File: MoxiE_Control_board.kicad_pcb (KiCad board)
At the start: 2 copper layers, 90 x 50 mm, 144 parts, among them J101 USB_B_Micro, J301 SWD, J401 Conn_01x02, J402 Conn_01x02, J403 Conn_01x02, K101 SERVO, P101 CANBUS, P102 Serial3, P103 CTRL_SIGNALS, P104 SPI, P105 Serial1/tim4, P106 I2C, P107 HALL/Encoder, Q401 IRLML6344TRPBF, Q402 IRLML6344TRPBF, Q701 TPH2R608NH,L1Q, Q702 TPH2R608NH,L1Q, Q703 TPH2R608NH,L1Q, Q704 TPH2R608NH,L1Q, Q801 TPH2R608NH,L1Q, Q802 TPH2R608NH,L1Q, Q803 TPH2R608NH,L1Q, Q804 TPH2R608NH,L1Q, Q901 TPH2R608NH,L1Q, Q902 TPH2R608NH,L1Q, Q903 TPH2R608NH,L1Q, Q904 TPH2R608NH,L1Q, U201 TJA1051TK-3, U301 STM32F40X_LQFP64, U501 TPS561201, U601 DRV8353RSRGZT, X301 8MHz 10ppm

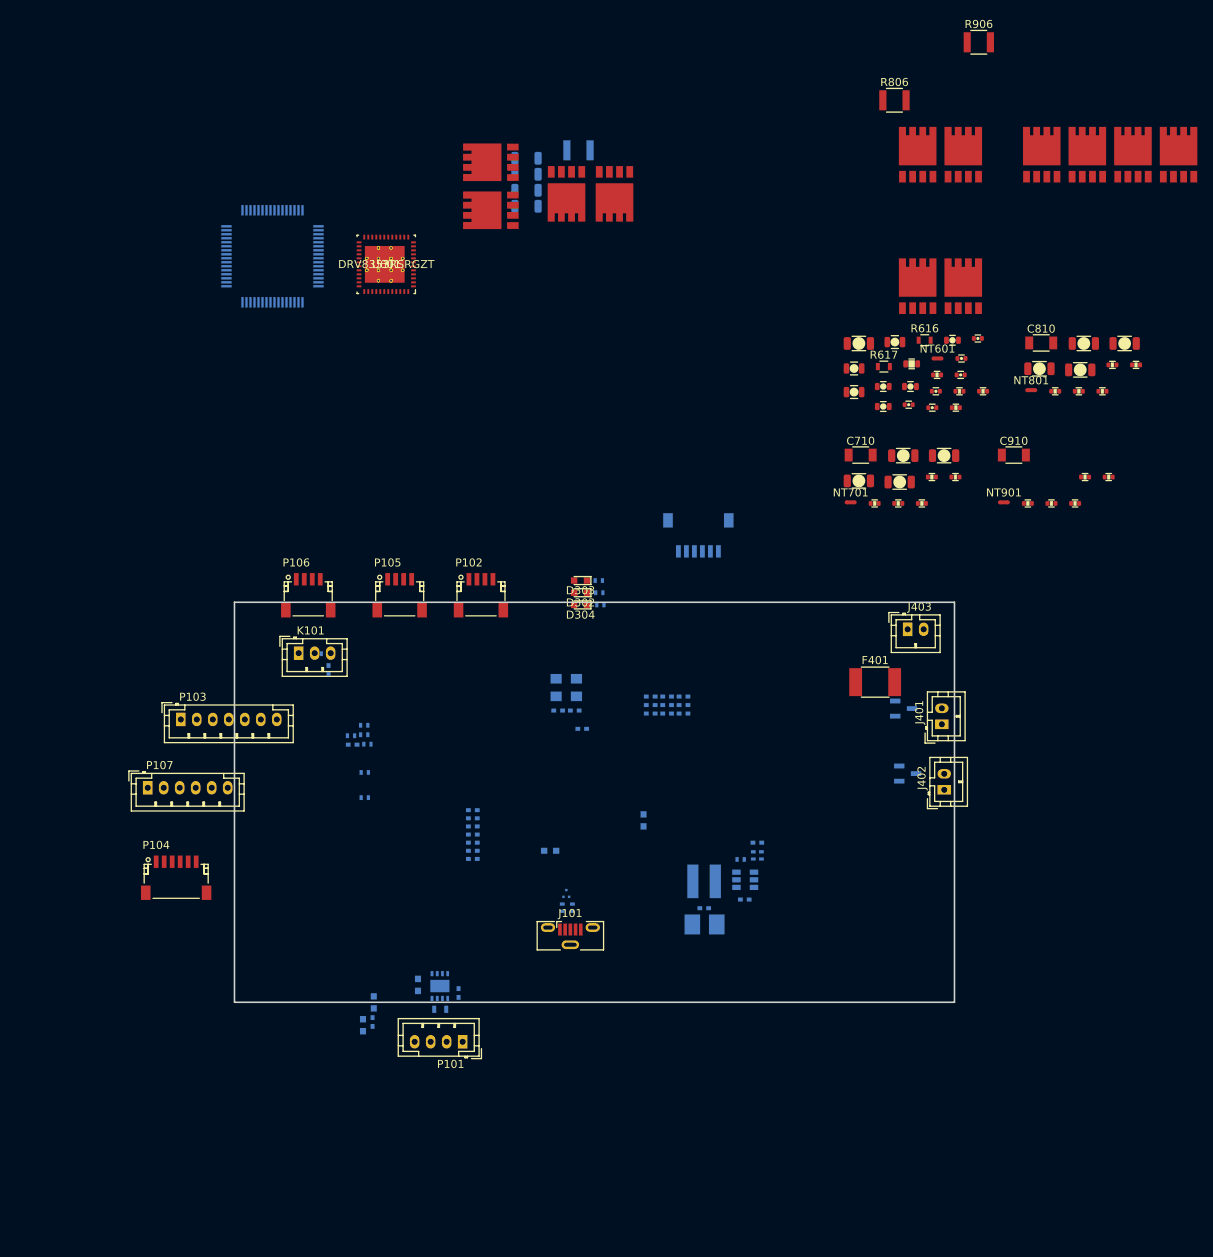
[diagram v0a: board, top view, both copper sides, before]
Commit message: further progress finalising schematic and power stage laied out. drv is fanned out, and logic is starting to be routed
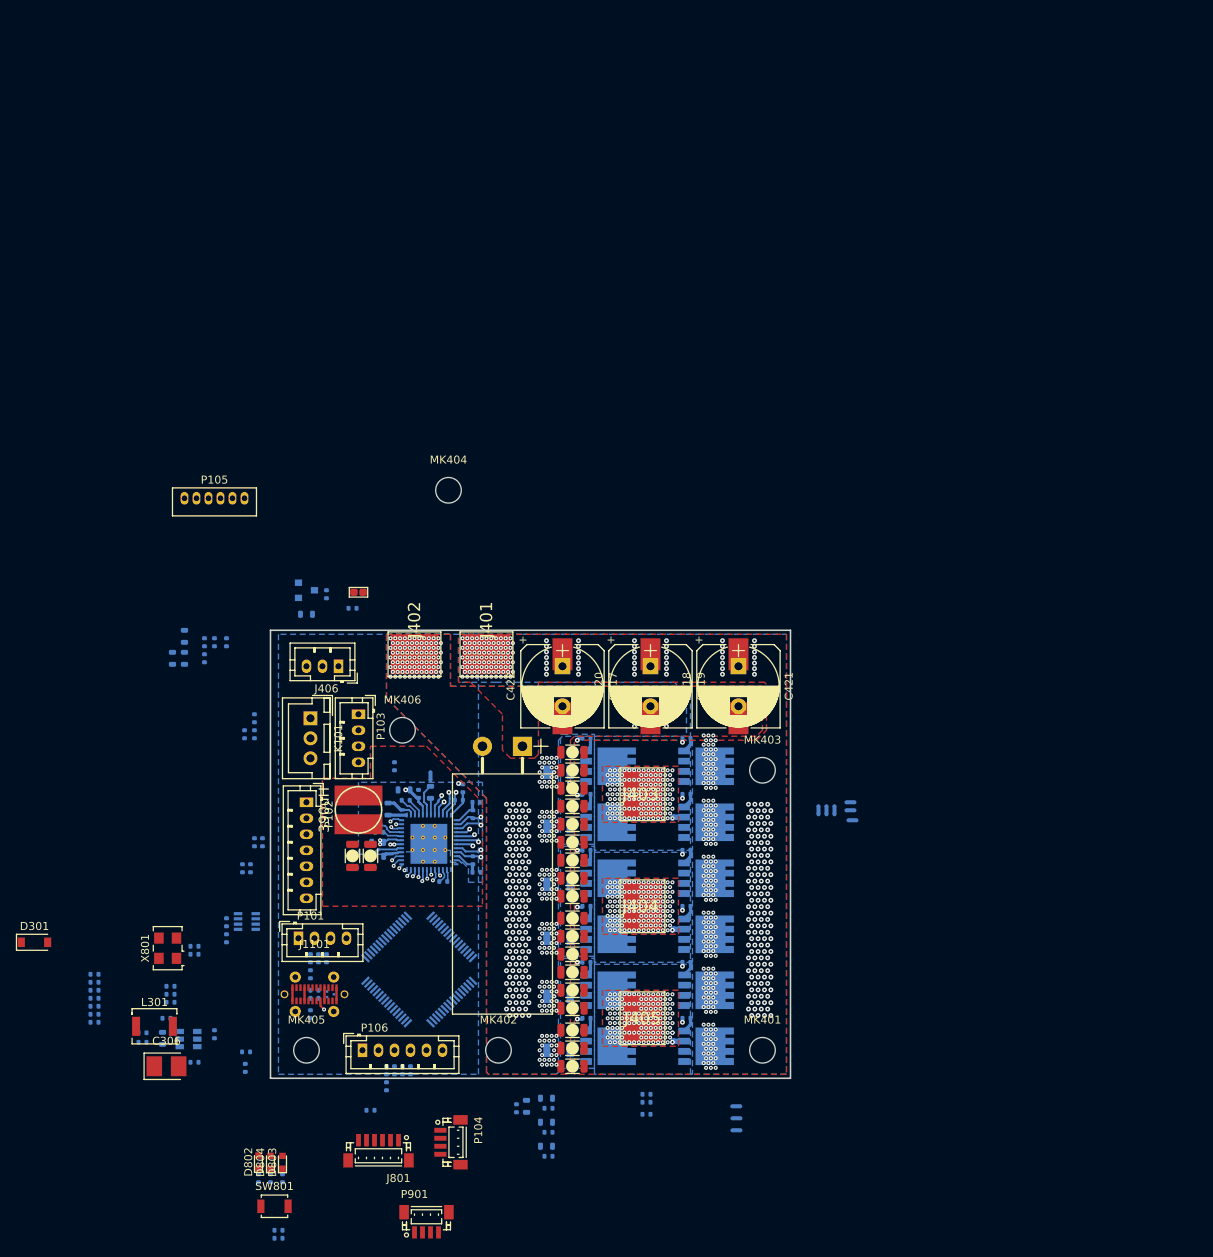
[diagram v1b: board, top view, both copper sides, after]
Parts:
- removed C103, C104, C105: 4.7nf, Capacitors_SMD:C_0402
- removed C106, C107, C108, C109, C111: 100nf, Capacitors_SMD:C_0402
- removed C110: 100n, Capacitors_SMD:C_0402
- removed C308: 15p, Capacitors_SMD:C_0402
- removed C309, C310, C311, C312: 2.2u, Capacitors_SMD:C_0402
- removed C623: 10uF, pkl_dipol:C_0805
- removed C624: 1.5uF, pkl_dipol:C_1206
- removed C625: 0.1uF, pkl_dipol:C_0603
- removed C626: 0.1uF, pkl_dipol:C_0805
- removed C627: 0.47uF, pkl_dipol:C_0402
- removed C629: 0.047uF, pkl_dipol:C_0402
- removed C630, C631, C633: 1uF, pkl_dipol:C_0603
- removed C632: 0.01uF, pkl_dipol:C_0402
- removed C634: 18nF, pkl_dipol:C_0402
- removed C635: 22uF, pkl_dipol:C_0805
- removed C710, C910: 100v_1.0uF, Capacitors_SMD:C_1206
- removed C902, C903, C904, C905: 1uF, pkl_dipol:C_1206
- removed D302: BLUE, LEDs:LED_0603
- removed D303: GREEN, LEDs:LED_0603
- removed D304: RED, LEDs:LED_0603
- removed F401: 0.5A polyfuse, Resistors_SMD:R_1812
- removed J101: USB_B_Micro, Connectors_USB:USB_Micro-B_Vertical_Molex-105133-0001
- removed J301: SWD, Connectors_JST:JST_SH_SM06B-SRSS-TB_06x1.00mm_Angled
- removed L501: 3.3uH, Mas_custom_parts:L_Bourns_SRN-4018
- removed NT801, NT901: Net-Tie_2, NetTie:NetTie-2_SMD_Pad0.5mm
- removed P107: HALL/Encoder, Connectors_JST:JST_PH_B6B-PH-K_06x2.00mm_Straight
- removed Q402: IRLML6344TRPBF, digikey-footprints:SOT-23-3
- removed Q802, Q901, Q902, Q903, Q904: TPH2R608NH,L1Q, moxie-drive-custom:SOP8_Advance
- removed R105: 22R, Resistors_SMD:R_0402
- removed R106: 2k2, Resistors_SMD:R_0402
- removed the R502 at (164.9, 131.6)
- removed the R503 at (165.9, 131.6)
- removed the R603 at (190.2, 75.7)
- removed R616: 39k, Resistors_SMD:R_0603
- removed R617: 2k2, Resistors_SMD:R_0603
- removed the R703 at (183.0, 87.6)
- removed R805, R901, R902, R904, R905: 5Ω, pkl_dipol:R_0402
- removed R806, R906: 0.5mΩ, Resistors_SMD:R_1210
- removed R903: 100Ω, pkl_dipol:R_0402
- removed U501: TPS561201, TO_SOT_Packages_SMD:SOT-23-6
- removed U601: DRV8353RSRGZT, Locals:DRV8353RHRGZR
- removed X301: 8MHz 10ppm, Oscillators:Oscillator_SMD_EuroQuartz_XO53-4pin_5.0x3.2mm
- added C401: 10uF, pkl_dipol:C_0603, B.Cu at (121.2, 123.5)
- added C402: 10uF, pkl_dipol:C_0603, B.Cu at (93.8, 107.0)
- added C403: 0.1uF, pkl_dipol:C_0402, B.Cu at (123.0, 124.0)
- added C404: 0.1uF, pkl_dipol:C_0603, B.Cu at (117.9, 130.0)
- added C405: 0.47uF, pkl_dipol:C_0402, B.Cu at (118.1, 128.8)
- added C406: 0.1uF, pkl_dipol:C_0402, B.Cu at (126.1, 134.9)
- added C407: 0.047uF, pkl_dipol:C_0402, B.Cu at (121.4, 124.8)
- added C408: 1uF, pkl_dipol:C_0603, B.Cu at (119.2, 125.8)
- added C409: 1uF, pkl_dipol:C_0603, B.Cu at (117.9, 131.8)
- added C410: 0.01uF, pkl_dipol:C_0402, B.Cu at (117.8, 127.8)
- added C411: 1uF, pkl_dipol:C_0603, B.Cu at (124.5, 123.8)
- added C412: 18nF, pkl_dipol:C_0402, B.Cu at (97.5, 105.0)
- added C413: 10uF, pkl_dipol:C_0603, B.Cu at (92.2, 107.0)
- added C414: 560uF, moxie-drive-custom:CP_Radial_D12.5mm_P5.00mm_horiz, F.Cu at (136.0, 118.0)
- added C417: 56uF, Capacitors_THT:CP_Radial_D10.0mm_P5.00mm, F.Cu at (141.0, 108.0)
- added C418: 20uF, Capacitors_SMD:CP_Elec_10x10.5, F.Cu at (163.0, 110.5)
- added C419: 56uF, Capacitors_THT:CP_Radial_D10.0mm_P5.00mm, F.Cu at (152.0, 108.0)
- added C420: 20uF, Capacitors_SMD:CP_Elec_10x10.5, F.Cu at (152.0, 110.5)
- added C421: 56uF, Capacitors_THT:CP_Radial_D10.0mm_P5.00mm, F.Cu at (163.0, 108.0)
- added C422: 20uF, Capacitors_SMD:CP_Elec_10x10.5, F.Cu at (141.0, 110.5)
- added C423: 100nf, pkl_dipol:C_0402, B.Cu at (151.5, 161.5)
- added C424: 1uF, pkl_dipol:C_1206, F.Cu at (117.0, 131.7)
- added C425: 1uF, pkl_dipol:C_1206, F.Cu at (114.8, 131.7)
- added C601: 2.2nF, pkl_dipol:C_0402, B.Cu at (129.8, 126.5)
- added C605: 1uF, pkl_dipol:C_1206, F.Cu at (142.2, 139.5)
- added C606: 1uF, pkl_dipol:C_1206, F.Cu at (142.2, 134.5)
- added C607: 1uF, pkl_dipol:C_1206, F.Cu at (142.2, 136.8)
- added C701: 2.2nF, pkl_dipol:C_0402, B.Cu at (128.1, 124.8)
- added C702: 1uF, pkl_dipol:C_1206, F.Cu at (142.2, 118.8)
- added C703: 1uF, pkl_dipol:C_1206, F.Cu at (142.2, 127.8)
- added C704: 1uF, pkl_dipol:C_1206, F.Cu at (142.2, 130.0)
- added C706: 1uF, pkl_dipol:C_1206, F.Cu at (142.2, 121.0)
- added C707: 1uF, pkl_dipol:C_1206, F.Cu at (142.2, 123.2)
- added C801: 2.2u, pkl_dipol:C_0402, B.Cu at (101.5, 156.2)
- added C806: 15p, pkl_dipol:C_0402, B.Cu at (95.0, 143.0)
- added C807: 2.2u, pkl_dipol:C_0402, B.Cu at (82.5, 149.5)
- added C808: 15p, pkl_dipol:C_0402, B.Cu at (95.0, 144.0)
- added C809: 2.2u, pkl_dipol:C_0402, B.Cu at (82.5, 150.5)
- added C811: 2.2u, pkl_dipol:C_0402, B.Cu at (82.5, 146.5)
- added C812: 2.2u, pkl_dipol:C_0402, B.Cu at (82.5, 147.5)
- added C813: 100n, pkl_dipol:C_0402, B.Cu at (105.5, 179.5)
- added D1101: TPD2EUSB30DRTR, digikey-footprints:SOT-3, B.Cu at (112.0, 149.0)
- added D401: DFLS1100-7, Diodes_SMD:D_SOD-123, B.Cu at (116.0, 125.8)
- added D802: BLUE, LEDs:LED_0603, F.Cu at (103.0, 170.0)
- added D803: GREEN, LEDs:LED_0603, F.Cu at (106.0, 170.0)
- added D804: RED, LEDs:LED_0603, F.Cu at (104.5, 170.0)
- added J1101: USB_C_Receptacle, pkl_connectors:USB_C_receptacle_vertical, F.Cu at (110.0, 149.0)
- added J404: B, crf1:1PAD_6x5mm, F.Cu at (151.0, 138.0)
- added J405: C, crf1:1PAD_6x5mm, F.Cu at (151.0, 152.0)
- added J406: Conn_01x03, Connectors_JST:JST_PH_B3B-PH-K_03x2.00mm_Straight, F.Cu at (113.0, 108.0)
- added J801: SWD, Connectors_JST:JST_SH_BM06B-SRSS-TB_06x1.00mm_Straight, F.Cu at (118.0, 168.5)
- added JP401: pwr_ctl_byp, pkl_jumpers:J_0603, F.Cu at (115.5, 98.8)
- added L301: 3.3uH, Inductors_SMD:L_Neosid_Ms42, F.Cu at (90.0, 153.0)
- added L401: 390uH, crf1:inductor_smd_5.8mmx4.8hmm, F.Cu at (115.5, 125.9)
- added MK401: Mounting_Hole, Mounting_Holes:MountingHole_3.2mm_M3_DIN965, F.Cu at (166.0, 156.0)
- added MK402: Mounting_Hole, Mounting_Holes:MountingHole_3.2mm_M3_DIN965, F.Cu at (133.0, 156.0)
- added MK403: Mounting_Hole, Mounting_Holes:MountingHole_3.2mm_M3_DIN965, F.Cu at (166.0, 121.0)
- added MK404: Mounting_Hole, Mounting_Holes:MountingHole_3.2mm_M3_DIN965, F.Cu at (126.8, 86.0)
- added MK405: Mounting_Hole, Mounting_Holes:MountingHole_3.2mm_M3_DIN965, F.Cu at (109.0, 156.0)
- added MK406: Mounting_Hole, Mounting_Holes:MountingHole_3.2mm_M3_DIN965, F.Cu at (121.0, 116.0)
- added NT401: Net-Tie_2, NetTie:NetTie-2_SMD_Pad0.5mm, B.Cu at (162.8, 164.5)
- added NT402: Net-Tie_2, NetTie:NetTie-2_SMD_Pad0.5mm, B.Cu at (162.7, 163.0)
- added NT403: Net-Tie_2, NetTie:NetTie-2_SMD_Pad0.5mm, B.Cu at (162.8, 166.0)
- added NT404: Net-Tie_2, NetTie:NetTie-2_SMD_Pad0.5mm, B.Cu at (124.5, 121.8)
- added NT501: Net-Tie_2, NetTie:NetTie-2_SMD_Pad0.5mm, B.Cu at (177.0, 126.0)
- added NT502: Net-Tie_2, NetTie:NetTie-2_SMD_Pad0.5mm, B.Cu at (173.0, 126.0)
- added NT503: Net-Tie_2, NetTie:NetTie-2_SMD_Pad0.5mm, B.Cu at (139.5, 149.2)
- added NT602: Net-Tie_2, NetTie:NetTie-2_SMD_Pad0.5mm, B.Cu at (174.0, 126.0)
- added NT603: Net-Tie_2, NetTie:NetTie-2_SMD_Pad0.5mm, B.Cu at (139.5, 128.0)
- added NT702: Net-Tie_2, NetTie:NetTie-2_SMD_Pad0.5mm, B.Cu at (175.0, 126.0)
- added NT703: Net-Tie_2, NetTie:NetTie-2_SMD_Pad0.5mm, B.Cu at (139.5, 121.2)
- added P901: I2C, Connectors_JST:JST_SH_BM04B-SRSS-TB_04x1.00mm_Straight, F.Cu at (124.0, 177.5)
- added Q501: TPH2R608NH,L1Q, moxie-drive-custom:SOP8_Advance, B.Cu at (159.5, 148.5)
- added Q502: TPH2R608NH,L1Q, moxie-drive-custom:SOP8_Advance, B.Cu at (147.2, 148.5)
- added Q503: TPH2R608NH,L1Q, moxie-drive-custom:SOP8_Advance, B.Cu at (159.5, 155.5)
- added Q504: TPH2R608NH,L1Q, moxie-drive-custom:SOP8_Advance, B.Cu at (147.2, 155.5)
- added Q702: TPH2R608NH,L1Q, moxie-drive-custom:SOP8_Advance, B.Cu at (147.2, 120.5)
- added R110: 10kΩ, pkl_dipol:R_0402, B.Cu at (119.0, 158.5)
- added R1101: 22R, pkl_dipol:R_0402, B.Cu at (110.0, 149.5)
- added R1102: 22R, pkl_dipol:R_0402, B.Cu at (110.0, 148.5)
- added R1103: 5.1k, pkl_dipol:R_0402, B.Cu at (109.5, 151.5)
- added R1104: 5.1k, pkl_dipol:R_0402, B.Cu at (109.5, 146.5)
- added R202: 120R, pkl_dipol:R_0402, B.Cu at (110.5, 144.5)
- added R203: 0R, pkl_dipol:R_0402, B.Cu at (99.0, 142.0)
- added R401: 1kOhm, pkl_dipol:C_0402, B.Cu at (101.0, 133.2)
- added R402: 10kΩ, pkl_dipol:C_0402, B.Cu at (102.0, 133.2)
- added R403: 560kΩ, pkl_dipol:R_0402, B.Cu at (120.0, 120.5)
- added R404: 200kΩ, pkl_dipol:R_0402, B.Cu at (99.0, 105.0)
- added R405: 5.1kΩ, pkl_dipol:R_0402, B.Cu at (96.2, 105.0)
- added R406: 1.0kΩ, pkl_dipol:R_0402, B.Cu at (96.2, 107.0)
- added R407: 910mΩ, pkl_dipol:R_0603, B.Cu at (93.8, 104.2)
- added R408: 47kΩ, pkl_dipol:R_0603, B.Cu at (139.0, 168.0)
- added R409: 2.2kΩ, pkl_dipol:R_0402, B.Cu at (139.2, 169.2)
- added R410: 47kΩ, pkl_dipol:R_0603, B.Cu at (139.0, 165.0)
- added R411: 2.2kΩ, pkl_dipol:R_0402, B.Cu at (139.2, 166.2)
- added R412: 47kΩ, pkl_dipol:R_0603, B.Cu at (139.0, 162.0)
- added R413: 2.2kΩ, pkl_dipol:R_0402, B.Cu at (139.2, 163.2)
- added R414: 47kΩ, pkl_dipol:R_0603, B.Cu at (136.5, 163.0)
- added R415: 2.2kΩ, pkl_dipol:R_0402, B.Cu at (135.2, 163.2)
- added R416: 10kΩ, pkl_dipol:R_0402, B.Cu at (151.5, 162.5)
- added R417: NTC 10kΩ, pkl_dipol:R_0402, B.Cu at (151.5, 164.0)
- added R418: 10k, pkl_dipol:R_0402, B.Cu at (111.5, 99.0)
- added R419: 500k, pkl_dipol:R_0603, B.Cu at (109.0, 101.5)
- added R420: 100, pkl_dipol:R_0402, B.Cu at (114.8, 100.8)
- added R506: 1mΩ, Resistors_SMD:R_1206, B.Cu at (140.5, 156.0)
- added R507: 1mΩ, Resistors_SMD:R_1206, B.Cu at (140.5, 149.2)
- added R601: 100Ω, pkl_dipol:R_0402, B.Cu at (130.2, 125.0)
- added R701: 100Ω, pkl_dipol:R_0402, B.Cu at (128.6, 123.2)
- added R705: 5Ω, pkl_dipol:R_0402, B.Cu at (144.0, 124.0)
- added R707: 1mΩ, Resistors_SMD:R_1206, B.Cu at (140.5, 121.2)
- added R801: 1k, pkl_dipol:R_0402, B.Cu at (103.0, 172.0)
- added R802: 1k, pkl_dipol:R_0402, B.Cu at (106.0, 172.0)
- added R804: 10k, pkl_dipol:R_0402, B.Cu at (105.5, 178.5)
- added SW801: SW_Push, Buttons_Switches_SMD:SW_SPST_B3U-1000P, F.Cu at (105.0, 175.5)
- added U401: DRV8353RSRGZT, Locals:DRV8353RHRGZR, B.Cu at (124.3, 130.0)
- added U801: STM32F40X_LQFP64, crf1:lqfp64_pad_mod, B.Cu at (123.1, 145.9)
- added X801: 8MHz 10ppm, Oscillators:Oscillator_SMD_EuroQuartz_XO53-4pin_5.0x3.2mm, F.Cu at (91.7, 143.2)
- C101: footprint Capacitors_SMD:C_0402 -> pkl_dipol:C_0402
- C102: value 100nf -> 100n; footprint Capacitors_SMD:C_0402 -> pkl_dipol:C_0402
- C201: value 2.2u -> 4.7nf; footprint Capacitors_SMD:C_0603 -> pkl_dipol:C_0402
- C202: value 100nf -> 2.2u; footprint Capacitors_SMD:C_0402 -> pkl_dipol:C_0402
- C301: value 2.2u -> 10uf; footprint Capacitors_SMD:C_0603 -> pkl_dipol:C_0603
- C302: value 2.2u -> 100nf; footprint Capacitors_SMD:C_0402 -> pkl_dipol:C_0402
- C303: value 2.2u -> 100nf; footprint Capacitors_SMD:C_0603 -> pkl_dipol:C_0402
- C304: value 100n -> 100nf; footprint Capacitors_SMD:C_0402 -> pkl_dipol:C_0402
- C305: value 2.2u -> 2.2uf; footprint Capacitors_SMD:C_0402 -> pkl_dipol:C_0402
- C306: value 15p -> 100uf; footprint Capacitors_SMD:C_0402 -> Capacitors_Tantalum_SMD:CP_Tantalum_Case-B_EIA-3528-21_Reflow; moved to F.Cu
- C307: value 2.2u -> NP; footprint Capacitors_SMD:C_0402 -> pkl_dipol:C_0402
- C501: value 2.2uf -> 2.2nF; footprint Capacitors_SMD:C_0603 -> pkl_dipol:C_0402
- C502, C503, C504: value 100nf -> 1uF; footprint Capacitors_SMD:C_0402 -> pkl_dipol:C_1206; moved to F.Cu
- C505: value 2.2uf -> 1uF; footprint Capacitors_SMD:C_0603 -> pkl_dipol:C_1206; moved to F.Cu
- C506: value 100uf -> 1uF; footprint Capacitors_Tantalum_SMD:CP_Tantalum_Case-B_EIA-3528-21_Reflow -> pkl_dipol:C_1206; moved to F.Cu
- C507: value NP -> 1uF; footprint Capacitors_SMD:C_0402 -> pkl_dipol:C_1206; moved to F.Cu
- C602: renamed from C702; value 1uF -> 1uF
- C603: renamed from C703; value 1uF -> 1uF
- C604: renamed from C704; value 1uF -> 1uF
- C705: value 1uF -> 1uF
- C802, C803, C805: value 1uF -> 2.2u; footprint pkl_dipol:C_1206 -> pkl_dipol:C_0402; moved to B.Cu
- C804: value 1uF -> 100n; footprint pkl_dipol:C_1206 -> pkl_dipol:C_0402; moved to B.Cu
- C810: value 100v_1.0uF -> 2.2u; footprint Capacitors_SMD:C_1206 -> pkl_dipol:C_0402; moved to B.Cu
- D301: value TPD2EUSB30DRTR -> 1.5KExxA; footprint digikey-footprints:SOT-3 -> Diodes_SMD:D_SOD-123; moved to F.Cu
- J401: value Conn_01x02 -> +Vbat; footprint Connectors_JST:JST_PH_B2B-PH-K_02x2.00mm_Straight -> crf1:1PAD_6x5mm
- J402: value Conn_01x02 -> Gnd; footprint Connectors_JST:JST_PH_B2B-PH-K_02x2.00mm_Straight -> crf1:1PAD_6x5mm
- J403: value Conn_01x02 -> A; footprint Connectors_JST:JST_PH_B2B-PH-K_02x2.00mm_Straight -> crf1:1PAD_6x5mm
- K101: footprint Connectors_JST:JST_PH_B3B-PH-K_03x2.00mm_Straight -> Connectors_JST:JST_XH_B03B-XH-A_03x2.50mm_Straight
- NT601, NT701: moved to B.Cu
- P102: value Serial3 -> CTRL_SIGNALS; footprint Connectors_JST:JST_SH_SM04B-SRSS-TB_04x1.00mm_Angled -> Connectors_JST:JST_PH_B7B-PH-K_07x2.00mm_Straight
- P103: value CTRL_SIGNALS -> Serial1/tim4; footprint Connectors_JST:JST_PH_B7B-PH-K_07x2.00mm_Straight -> Connectors_JST:JST_PH_B4B-PH-K_04x2.00mm_Straight
- P104: value SPI -> I2C; footprint Connectors_JST:JST_SH_SM06B-SRSS-TB_06x1.00mm_Angled -> Connectors_JST:JST_SH_BM04B-SRSS-TB_04x1.00mm_Straight
- P105: value Serial1/tim4 -> HALL/Encoder; footprint Connectors_JST:JST_SH_SM04B-SRSS-TB_04x1.00mm_Angled -> crf1:simple_jst-zh_1.5mm_unfinished
- P106: value I2C -> HALL/Encoder; footprint Connectors_JST:JST_SH_SM04B-SRSS-TB_04x1.00mm_Angled -> Connectors_JST:JST_PH_B6B-PH-K_06x2.00mm_Straight
- Q401: value IRLML6344TRPBF -> Q_PNP_BCE; footprint digikey-footprints:SOT-23-3 -> TO_SOT_Packages_SMD:SOT-23
- Q601: renamed from Q701; moved to B.Cu
- Q602: renamed from Q702; moved to B.Cu
- Q603: renamed from Q703; moved to B.Cu
- Q604: renamed from Q704; moved to B.Cu
- Q701: renamed from Q801; moved to B.Cu
- Q703: renamed from Q803; moved to B.Cu
- Q704: renamed from Q804; moved to B.Cu
- R101: value 100R -> 0Ω; footprint Resistors_SMD:R_0402 -> pkl_dipol:R_0402
- R102: value 100k -> 100Ω; footprint Resistors_SMD:R_0402 -> pkl_dipol:R_0402
- R103: value 100k -> 100kΩ; footprint Resistors_SMD:R_0402 -> pkl_dipol:R_0402
- R104: value 22R -> 100kΩ; footprint Resistors_SMD:R_0402 -> pkl_dipol:R_0402
- R107, R108: value 2k2 -> 2k2Ω; footprint Resistors_SMD:R_0402 -> pkl_dipol:R_0402
- R109: value 10k -> 2k2Ω; footprint Resistors_SMD:R_0402 -> pkl_dipol:R_0402
- R201: value 220R -> 120R; footprint Resistors_SMD:R_0603 -> pkl_dipol:R_0402
- R301: footprint Resistors_SMD:R_0402 -> pkl_dipol:R_0402
- R302: value 1k -> R33.2k 0.1%; footprint Resistors_SMD:R_0402 -> pkl_dipol:R_0402
- R303: value 1k -> 10k 0.1%; footprint Resistors_SMD:R_0402 -> pkl_dipol:R_0402
- R501: value 1k -> 100Ω; footprint Resistors_SMD:R_0402 -> pkl_dipol:R_0402
- R502: renamed from R601; value 1kOhm -> 5Ω; footprint pkl_dipol:C_0402 -> pkl_dipol:R_0402; moved to B.Cu
- R503: renamed from R602; value 10kOhm -> 5Ω; footprint pkl_dipol:C_0402 -> pkl_dipol:R_0402; moved to B.Cu
- R504: renamed from R604; value 200kOhm -> 5Ω; moved to B.Cu
- R505: renamed from R605; value 5.1kOhm -> 5Ω; moved to B.Cu
- R602: renamed from R701; moved to B.Cu
- R603: renamed from R702; moved to B.Cu
- R604: renamed from R704; moved to B.Cu
- R605: renamed from R705; moved to B.Cu
- R606: value 1.0kOhm -> 1mΩ; footprint pkl_dipol:R_0402 -> Resistors_SMD:R_1206; moved to B.Cu
- R607: value 910mOhm -> 1mΩ; footprint pkl_dipol:R_0603 -> Resistors_SMD:R_1206; moved to B.Cu
- R702: renamed from R801; moved to B.Cu
- R703: renamed from R802; moved to B.Cu
- R704: renamed from R804; moved to B.Cu
- R706: value 0.5mΩ -> 1mΩ; footprint Resistors_SMD:R_1210 -> Resistors_SMD:R_1206
- R803: value 100Ω -> 1k; moved to B.Cu
- U201: value TJA1051TK-3 -> MAX3051; footprint Housings_DFN_QFN:DFN-8-1EP_3x3mm_Pitch0.65mm -> TO_SOT_Packages_SMD:SOT-23-8
- U301: value STM32F40X_LQFP64 -> TPS561201; footprint crf1:lqfp64_pad_mod -> TO_SOT_Packages_SMD:SOT-23-6
- moved C805 154.2 mm to (82.5, 152.5), turned to 180 degrees
- moved C810 143.4 mm to (82.5, 148.5), turned to 180 degrees
- moved C802 143.0 mm to (82.5, 151.5), turned to 180 degrees
- moved R803 141.0 mm to (104.5, 172.0), turned to 90 degrees
- moved C803 138.5 mm to (101.3, 158.2), turned to 270 degrees
- moved C804 128.2 mm to (117.0, 163.5)
- moved Q604 107.4 mm to (147.2, 141.5), turned to 90 degrees
- moved Q603 101.4 mm to (159.5, 141.5), turned to 90 degrees
- moved U301 98.4 mm to (94.2, 154.6)
- moved Q601 93.8 mm to (159.5, 134.5)
- moved R505 91.6 mm to (144.0, 152.0), turned to 180 degrees
- moved R504 86.7 mm to (156.5, 152.0), turned to 180 degrees
- moved Q602 85.2 mm to (147.2, 134.5), turned to 90 degrees
- moved R606 84.8 mm to (140.5, 142.0), turned to 180 degrees
- moved R706 84.5 mm to (140.5, 128.0)
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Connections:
- net /drv_power_stage/power_phase/H_GATE renamed /drv_power_stage/power_phase_B/H_GATE
- net /drv_power_stage/power_phase/L_GATE renamed /drv_power_stage/power_phase_B/L_GATE
- net /drv_power_stage/sheet5E9B1641/H_GATE renamed /drv_power_stage/power_phase_A/H_GATE
- net /sheet5B3977DF/CANH renamed /CAN_tranciever/CANH
- C101 pad 2: /sheet5B3977E0/SERVO -> /Microcontroller/SERVO
- C102 pad 1: /sheet5B3977E0/ADC_TEMP -> GND
- C102 pad 2: GND -> /Microcontroller/TEMP_MOTOR
- C201 pad 1: +5V -> Net-(C201-Pad1)
- C301 pad 1: GND -> +15V
- C301 pad 2: /sheet5B3977E0/VCAP2 -> GND
- C302 pad 1: GND -> +15V
- C302 pad 2: +3V3 -> GND
- C303 pad 1: GND -> Net-(C303-Pad1)
- C303 pad 2: /sheet5B3977E0/VCAP1 -> Net-(C303-Pad2)
- C304 pad 1: GND -> +3V3
- C304 pad 2: NRST -> GND
- C305 pad 1: GND -> +3V3
- C305 pad 2: +3V3 -> GND
- C306 pad 1: Net-(C306-Pad1) -> +3V3
- C307 pad 1: GND -> +3V3
- C307 pad 2: +3V3 -> Net-(C307-Pad2)
- C501 pad 1: +12V -> /drv_power_stage/power_phase_C/NR_SENSE
- C501 pad 2: GND -> /drv_power_stage/power_phase_C/PR_SENSE
- C502 pad 1: +12V -> +BATT
- C502 pad 2: GND -> GNDD
- C503 pad 1: Net-(C503-Pad1) -> +BATT
- C503 pad 2: Net-(C503-Pad2) -> GNDD
- C504 pad 1: +3V3 -> +BATT
- C504 pad 2: GND -> GNDD
- C505 pad 1: +3V3 -> +BATT
- C505 pad 2: GND -> GNDD
- C506 pad 1: +3V3 -> +BATT
- C506 pad 2: GND -> GNDD
- C507 pad 1: +3V3 -> +BATT
- C507 pad 2: Net-(C507-Pad2) -> GNDD
- C602 pad 2: GND -> GNDD
- C603 pad 2: GND -> GNDD
- C604 pad 2: GND -> GNDD
- C705 pad 2: GND -> GNDD
- C802 pad 1: +BATT -> GNDA
- C802 pad 2: GND -> +3V3
- C803 pad 1: +BATT -> GND
- C803 pad 2: GND -> /Microcontroller/VCAP1
- C804 pad 1: +BATT -> GND
- C804 pad 2: GND -> NRST
- C805 pad 1: +BATT -> GNDA
- C805 pad 2: GND -> +3V3
- C810 pad 1: +BATT -> GND
- C810 pad 2: GNDD -> +3V3
- D301 pad 1: /sheet5B3977E0/USB_DP -> +3V3
- D301 pad 2: /sheet5B3977E0/USB_DM -> GND
- J401 pad 1: Net-(F401-Pad2) -> +BATT
- J402 pad 1: Net-(F401-Pad2) -> GNDD
- J403 pad 1: Net-(F401-Pad2) -> /drv_power_stage/PHASE_A
- K101 pad 2: Net-(JP101-Pad2) -> Net-(K101-Pad2)
- NT601 pad 1: GNDD -> (no net)
- NT601 pad 2: GND -> (no net)
- NT701 pad 1: /drv_power_stage/power_phase/H_SWITCH -> (no net)
- NT701 pad 2: /drv_power_stage/power_phase/PHASE_OUT -> (no net)
- P101 pad 2: /sheet5B3977DF/CANL -> /CAN_tranciever/CANL
- P101 pad 4: Net-(P101-Pad4) -> (no net)
- P102 pad 1: /sheet5B3977E0/USART3_RX -> +3V3
- P102 pad 2: /sheet5B3977E0/USART3_TX -> GND
- P102 pad 3: +3V3 -> /Microcontroller/ADC_THROTTLE
- P102 pad 4: GND -> /Microcontroller/ADC_BRAKE
- P103 pad 1: +3V3 -> /Microcontroller/USART1_RX
- P103 pad 2: GND -> /Microcontroller/USART1_TX
- P103 pad 3: /sheet5B3977E0/ADC_THROTTLE -> +3V3
- P103 pad 4: /sheet5B3977E0/ADC_BRAKE -> GND
- P104 pad 1: +3V3 -> /Microcontroller/SCL_2
- P104 pad 2: /sheet5B3977E0/SPI3_MOSI -> /Microcontroller/SDA_2
- P104 pad 3: /sheet5B3977E0/SPI3_MISO -> +3V3
- P104 pad 4: /sheet5B3977E0/SPI3_SCK -> GND
- P105 pad 1: /sheet5B3977E0/USART1_RX -> (no net)
- P105 pad 2: /sheet5B3977E0/USART1_TX -> (no net)
- P105 pad 3: +3V3 -> (no net)
- P105 pad 4: GND -> (no net)
- P106 pad 1: /sheet5B3977E0/SCL_2 -> +3V3
- P106 pad 2: /sheet5B3977E0/SDA_2 -> /Microcontroller/TEMP_MOTOR
- P106 pad 3: +3V3 -> /Microcontroller/HALL_1
- P106 pad 4: GND -> /Microcontroller/HALL_2
- Q401 pad 1: /aux_outputs/AUX1_PWM -> /drv_power_stage/pwr_ctl_g
- Q401 pad 2: GNDD -> /drv_power_stage/batt_pwr_ctl
- Q401 pad 3: Net-(J401-Pad2) -> +BATT
- Q601 pad 3: /drv_power_stage/power_phase/PHASE_OUT -> /drv_power_stage/PHASE_B
- Q602 pad 1: /drv_power_stage/power_phase/PHASE_OUT -> /drv_power_stage/PHASE_B
- Q602 pad 3: Net-(Q702-Pad3) -> /drv_power_stage/power_phase_B/PR_SENSE
- Q603 pad 3: /drv_power_stage/power_phase/PHASE_OUT -> /drv_power_stage/PHASE_B
- Q604 pad 1: /drv_power_stage/power_phase/PHASE_OUT -> /drv_power_stage/PHASE_B
- Q604 pad 3: Net-(Q702-Pad3) -> /drv_power_stage/power_phase_B/PR_SENSE
- Q701 pad 3: /drv_power_stage/sheet5E9B1641/PHASE_OUT -> /drv_power_stage/PHASE_A
- Q703 pad 3: /drv_power_stage/sheet5E9B1641/PHASE_OUT -> /drv_power_stage/PHASE_A
- Q704 pad 1: /drv_power_stage/sheet5E9B1641/PHASE_OUT -> /drv_power_stage/PHASE_A
- Q704 pad 3: Net-(Q802-Pad3) -> /drv_power_stage/power_phase_A/PR_SENSE
- R101 pad 1: /sheet5B3977E0/SERVO -> Net-(K101-Pad2)
- R101 pad 2: Net-(K101-Pad1) -> +3V3
- R102 pad 1: /sheet5B3977E0/ADC_THROTTLE -> /Microcontroller/SERVO
- R102 pad 2: GND -> Net-(K101-Pad1)
- R103 pad 1: /sheet5B3977E0/ADC_BRAKE -> /Microcontroller/ADC_THROTTLE
- R104 pad 1: /sheet5B3977E0/USB_DP -> /Microcontroller/ADC_BRAKE
- R104 pad 2: Net-(J101-Pad3) -> GND
- R107 pad 1: /sheet5B3977E0/HALL_2 -> /Microcontroller/HALL_1
- R108 pad 1: /sheet5B3977E0/HALL_3 -> /Microcontroller/HALL_2
- R109 pad 1: /sheet5B3977E0/TEMP_MOTOR -> /Microcontroller/HALL_3
- R201 pad 2: /sheet5B3977DF/CANL -> Net-(C201-Pad1)
- R301 pad 1: Net-(D302-Pad1) -> Net-(R301-Pad1)
- R301 pad 2: +3V3 -> +15V
- R302 pad 1: Net-(D303-Pad1) -> +3V3
- R302 pad 2: /sheet5B3977E0/LED_GREEN -> Net-(C307-Pad2)
- R303 pad 1: Net-(D304-Pad1) -> Net-(C307-Pad2)
- R303 pad 2: /sheet5B3977E0/LED_RED -> GND
- R501 pad 1: Net-(R501-Pad1) -> /drv_power_stage/power_phase_C/NR_SENSE
- R501 pad 2: +12V -> /drv_power_stage/power_phase_C/NR_SENSE_R
- R502 pad 1: +3V3 -> Net-(Q501-Pad2)
- R502 pad 2: Net-(R601-Pad2) -> /drv_power_stage/power_phase_C/H_GATE
- R503 pad 1: +3V3 -> Net-(Q502-Pad2)
- R503 pad 2: /sheet5B3977E0/FAULT -> /drv_power_stage/power_phase_C/L_GATE
- R504 pad 1: GNDD -> Net-(Q503-Pad2)
- R504 pad 2: /drv_power_stage/buck_rcl -> /drv_power_stage/power_phase_C/H_GATE
- R505 pad 1: Net-(C634-Pad2) -> Net-(Q504-Pad2)
- R505 pad 2: /drv_power_stage/v_buck_sense -> /drv_power_stage/power_phase_C/L_GATE
- R606 pad 1: /drv_power_stage/v_buck_sense -> /drv_power_stage/power_phase_B/PR_SENSE
- R607 pad 1: Net-(C634-Pad2) -> /drv_power_stage/power_phase_B/PR_SENSE
- R607 pad 2: +12V -> GNDD
- R703 pad 2: /drv_power_stage/sheet5E9B1641/L_GATE -> /drv_power_stage/power_phase_A/L_GATE
- R706 pad 1: Net-(Q702-Pad3) -> /drv_power_stage/power_phase_A/PR_SENSE
- R706 pad 2: /drv_power_stage/power_phase/PR_SENSE -> GNDD
- R803 pad 1: /drv_power_stage/sheet5E9B1641/NR_SENSE -> Net-(D804-Pad1)
- R803 pad 2: Net-(R803-Pad2) -> /Microcontroller/LED_RED
- U201 pad 1: /sheet5B3977DF/CAN_TX -> /CAN_tranciever/CAN_TX
- U201 pad 3: +5V -> +3V3
- U201 pad 4: /sheet5B3977DF/CAN_RX -> /CAN_tranciever/CAN_RX
- U201 pad 5: +3V3 -> (no net)
- U201 pad 6: /sheet5B3977DF/CANL -> /CAN_tranciever/CANL
- U201 pad 8: GND -> Net-(R203-Pad1)
- U301 pad 1: +3V3 -> GND
- U301 pad 2: /sheet5B3977E0/REVERSE_SW -> Net-(C303-Pad1)
- U301 pad 3: /sheet5B3977E0/LED_GREEN -> +15V
- U301 pad 4: /sheet5B3977E0/LED_RED -> Net-(C307-Pad2)
- U301 pad 5: Net-(C306-Pad1) -> Net-(R301-Pad1)
- U301 pad 6: Net-(C308-Pad1) -> Net-(C303-Pad2)
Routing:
- net /drv_power_stage/power_phase_C/H_GATE: track 0.00 -> 27.8 mm, vias 0 -> 3
- net /drv_power_stage/power_phase_A/H_GATE: track 0.00 -> 27.7 mm, vias 0 -> 3
- net /drv_power_stage/power_phase_B/H_GATE: track 0.00 -> 27.3 mm, vias 0 -> 3
- net /drv_power_stage/PHASE_C: track 0.00 -> 13.7 mm, vias 0 -> 145
- net /drv_power_stage/PHASE_A: track 0.00 -> 13.4 mm, vias 0 -> 143
- net /drv_power_stage/PHASE_B: track 0.00 -> 13.4 mm, vias 0 -> 145
- net /drv_power_stage/power_phase_B/L_GATE: track 0.00 -> 11.9 mm, vias 0 -> 3
- net /drv_power_stage/power_phase_C/L_GATE: track 0.00 -> 11.8 mm, vias 0 -> 3
- net /drv_power_stage/power_phase_A/L_GATE: track 0.00 -> 11.6 mm, vias 0 -> 3
- net GND: track 0.00 -> 7.78 mm
- net +15V: track 0.00 -> 4.48 mm, vias 0 -> 1
- net /drv_power_stage/vdrain: track 0.00 -> 4.08 mm
- net /drv_power_stage/vgls: track 0.00 -> 3.71 mm
- net +BATT: track 0.00 -> 3.64 mm, vias 0 -> 465
- net /drv_power_stage/power_phase_B/NR_SENSE: track 0.00 -> 3.64 mm
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- added copper zone on B.Cu, net +BATT
- added copper zone on F.Cu, net +BATT
- added copper zone on In1.Cu, net +BATT
- added copper zone on In2.Cu, net +BATT
- added copper zone on B.Cu, net /drv_power_stage/PHASE_A
- added copper zone on F.Cu, net /drv_power_stage/PHASE_A
- added copper zone on In1.Cu, net /drv_power_stage/PHASE_A
- added copper zone on In2.Cu, net /drv_power_stage/PHASE_A
- added copper zone on B.Cu, net /drv_power_stage/PHASE_B
- added copper zone on F.Cu, net /drv_power_stage/PHASE_B
- added copper zone on In1.Cu, net /drv_power_stage/PHASE_B
- added copper zone on In2.Cu, net /drv_power_stage/PHASE_B
- added copper zone on B.Cu, net /drv_power_stage/PHASE_C
- added copper zone on F.Cu, net /drv_power_stage/PHASE_C
- added copper zone on In1.Cu, net /drv_power_stage/PHASE_C
- added copper zone on In2.Cu, net /drv_power_stage/PHASE_C
- added copper zone on B.Cu, net /drv_power_stage/power_phase_A/PR_SENSE
- added copper zone on B.Cu, net /drv_power_stage/power_phase_B/PR_SENSE
- added copper zone on B.Cu, net /drv_power_stage/power_phase_C/PR_SENSE
- added copper zone on B.Cu, net GND
- added copper zone on B.Cu, net GNDD
- added copper zone on F.Cu, net GNDD
- added copper zone on In1.Cu, net GNDD
- added copper zone on In2.Cu, net GNDD
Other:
- board size 90 x 50 mm -> 65 x 56 mm
- copper layers 2 -> 4
- net class Default: clearance 0.2 -> 0.18; via_drill 0.4 -> 0.3
- net class FLOAT_PWR added: clearance 0.2032, trace_width 0.24003, via_dia 0.6096, via_drill 0.254
- net class POWER added: clearance 0.25, trace_width 0.3, via_dia 0.8, via_drill 0.3
- rule trace_clearance: 0.2 -> 0.18
- rule trace_min: 0.2 -> 0.15
- rule via_min_drill: 0.3 -> 0.2
- board text added: "8mil via minimuse wicking, 10mil via best for currrent"
